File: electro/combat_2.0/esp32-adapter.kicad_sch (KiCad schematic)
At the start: 3 parts, among them J6 Conn_02x09_Odd_Even, J7 Conn_02x09_Odd_Even, U1 ESP32-WROOM-E

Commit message: almost ready pcb
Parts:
- renumbered J7 to J13, J6 to J14
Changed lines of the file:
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@@
   (symbol (lib_id "Connector_Generic:Conn_02x09_Odd_Even") (at 160.02 62.23 0) (unit 1)
     (in_bom yes) (on_board yes) (dnp no) (fields_autoplaced)
-    (property "Reference" "J6" (at 161.29 46.99 0)
+    (property "Reference" "J14" (at 161.29 46.99 0)
       (effects (font (size 1.27 1.27)))
     )
@@
       (project "combat_2.0"
         (path "/518cdd36-e3d2-496e-a534-90a14dea15b3/59dda071-b627-4862-8f7d-d7d020649f72"
-          (reference "J6") (unit 1)
+          (reference "J14") (unit 1)
         )
       )
@@
         )
         (path "/518cdd36-e3d2-496e-a534-90a14dea15b3/59dda071-b627-4862-8f7d-d7d020649f72"
-          (reference "U1") (unit 1)
+          (reference "U5") (unit 1)
         )
       )
@@
   (symbol (lib_id "Connector_Generic:Conn_02x09_Odd_Even") (at 49.53 60.96 0) (unit 1)
     (in_bom yes) (on_board yes) (dnp no) (fields_autoplaced)
-    (property "Reference" "J7" (at 50.8 45.72 0)
+    (property "Reference" "J13" (at 50.8 45.72 0)
       (effects (font (size 1.27 1.27)))
     )
@@
       (project "combat_2.0"
         (path "/518cdd36-e3d2-496e-a534-90a14dea15b3/59dda071-b627-4862-8f7d-d7d020649f72"
-          (reference "J7") (unit 1)
+          (reference "J13") (unit 1)
         )
       )

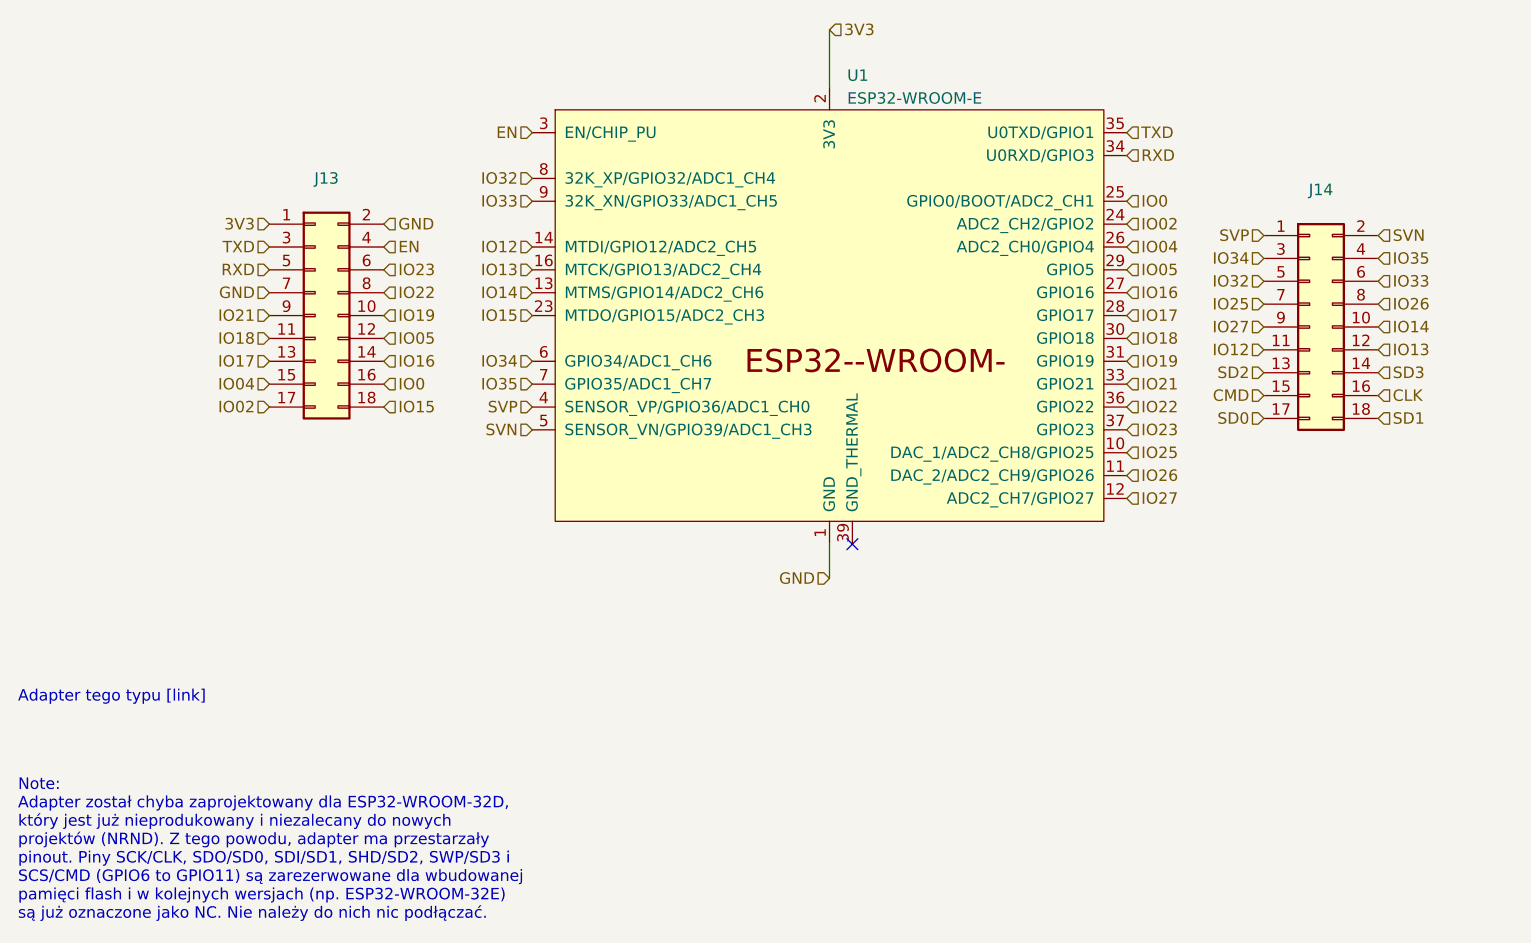
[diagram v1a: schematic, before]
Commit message: Change in mosfets routing
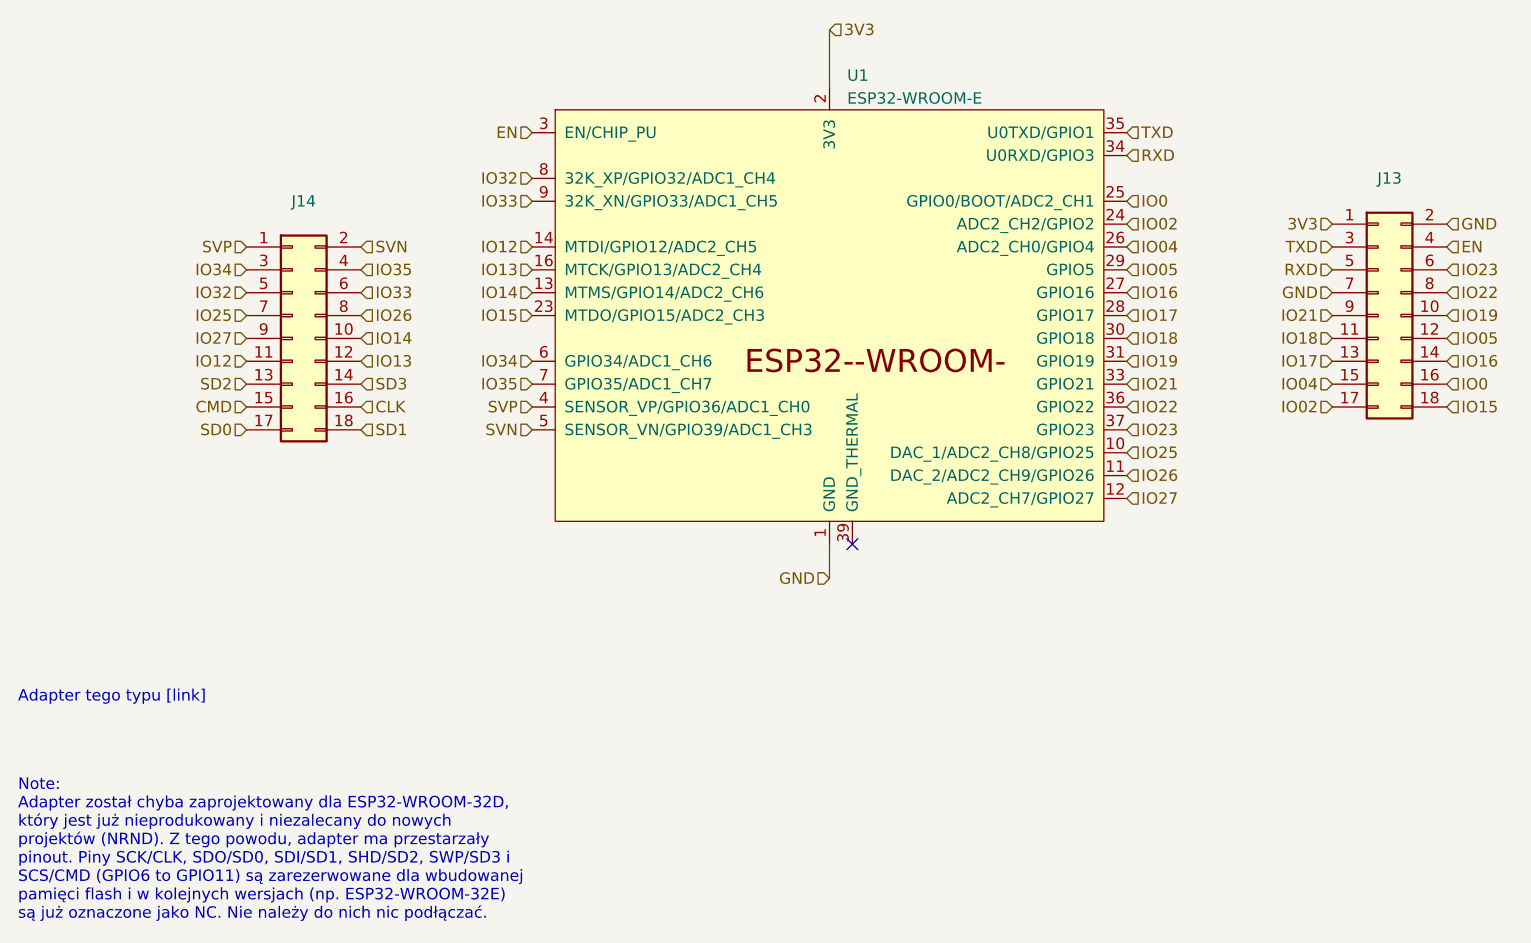
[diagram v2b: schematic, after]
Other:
- moved on the sheet: J13, J14
